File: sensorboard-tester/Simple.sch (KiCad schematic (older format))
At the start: 9 parts, among them J3 Sensor, J4 PTVoltage, J6 PTCurrent

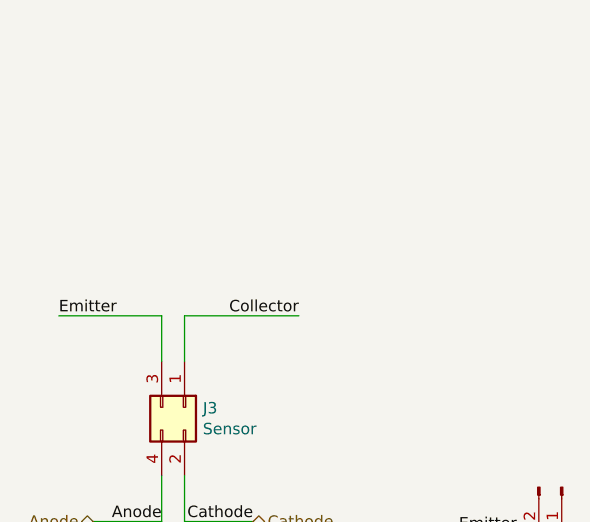
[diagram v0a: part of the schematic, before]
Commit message: Include mirrored headers for the sensorboards, in case their header has to be flipped.
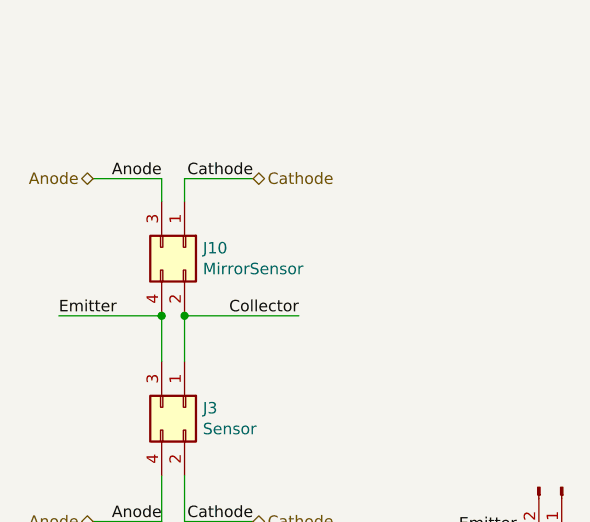
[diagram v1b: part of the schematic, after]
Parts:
- added J10: MirrorSensor, Pin_Headers:Pin_Header_Straight_2x02_Pitch2.54mm, symbol Connector_Generic:Conn_02x02_Odd_Even
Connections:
- net Anode: now also J10.3 (Pin_3)
- net Cathode: now also J10.1 (Pin_1)
- net Collector: now also J10.2 (Pin_2)
- net Emitter: now also J10.4 (Pin_4)
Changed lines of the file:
@@
 	5400 1450 5400 1250
 Connection ~ 5400 1450
+$Comp
+L Connector_Generic:Conn_02x02_Odd_Even J10
+U 1 1 5FE12BB4
+P 3600 2100
+F 0 "J10" V 3604 2180 50  0000 L CNN
+F 1 "MirrorSensor" V 3695 2180 50  0000 L CNN
+F 2 "Pin_Headers:Pin_Header_Straight_2x02_Pitch2.54mm" H 3600 2100 50  0001 C CNN
+F 3 "~" H 3600 2100 50  0001 C CNN
+	1    3600 2100
+	0    1    1    0
+$EndComp
+Connection ~ 3600 2400
+Connection ~ 3500 2400
+Wire Wire Line
+	3500 1900 3500 1800
+Wire Wire Line
+	3500 1800 3200 1800
+Wire Wire Line
+	3600 1900 3600 1800
+Wire Wire Line
+	3600 1800 3900 1800
+Text HLabel 3200 1800 0    50   BiDi ~ 0
+Anode
+Text HLabel 3900 1800 2    50   BiDi ~ 0
+Cathode
+Text Label 3900 1800 2    50   ~ 0
+Cathode
+Text Label 3500 1800 2    50   ~ 0
+Anode
 $EndSCHEMATC

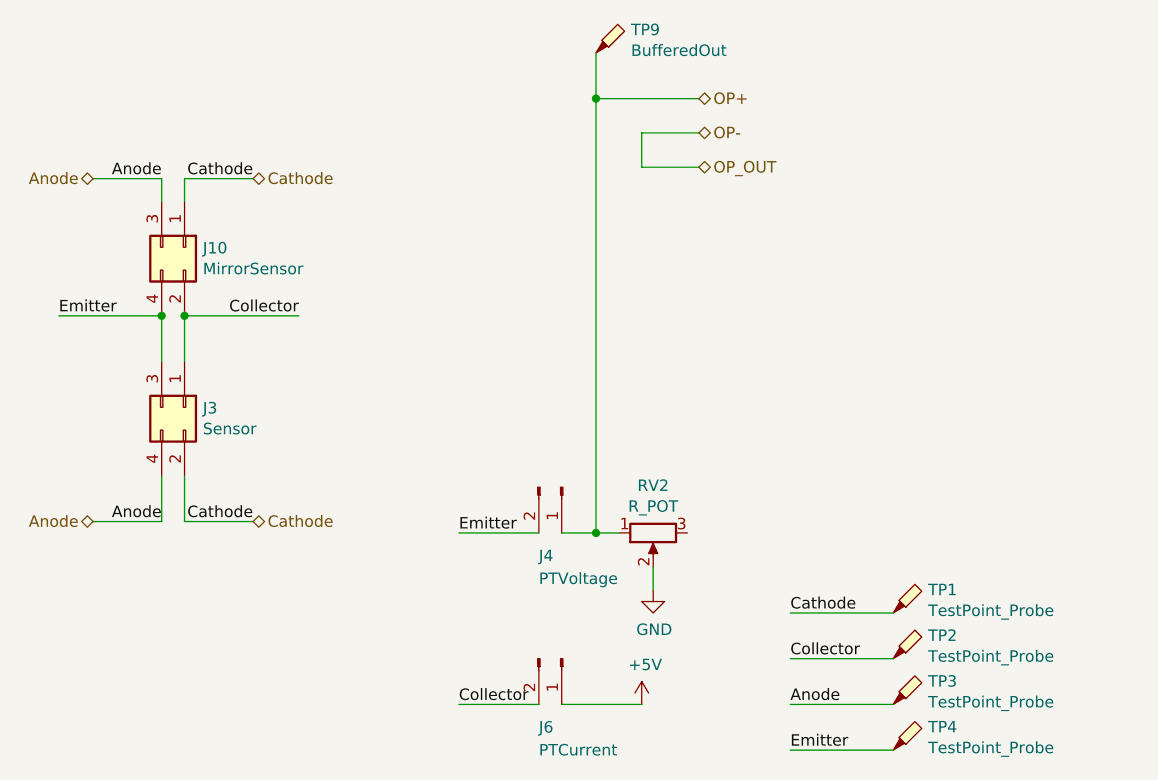
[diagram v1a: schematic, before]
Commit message: Cleanup and reconcile the headers. Switch to SOT23 regulators for both.
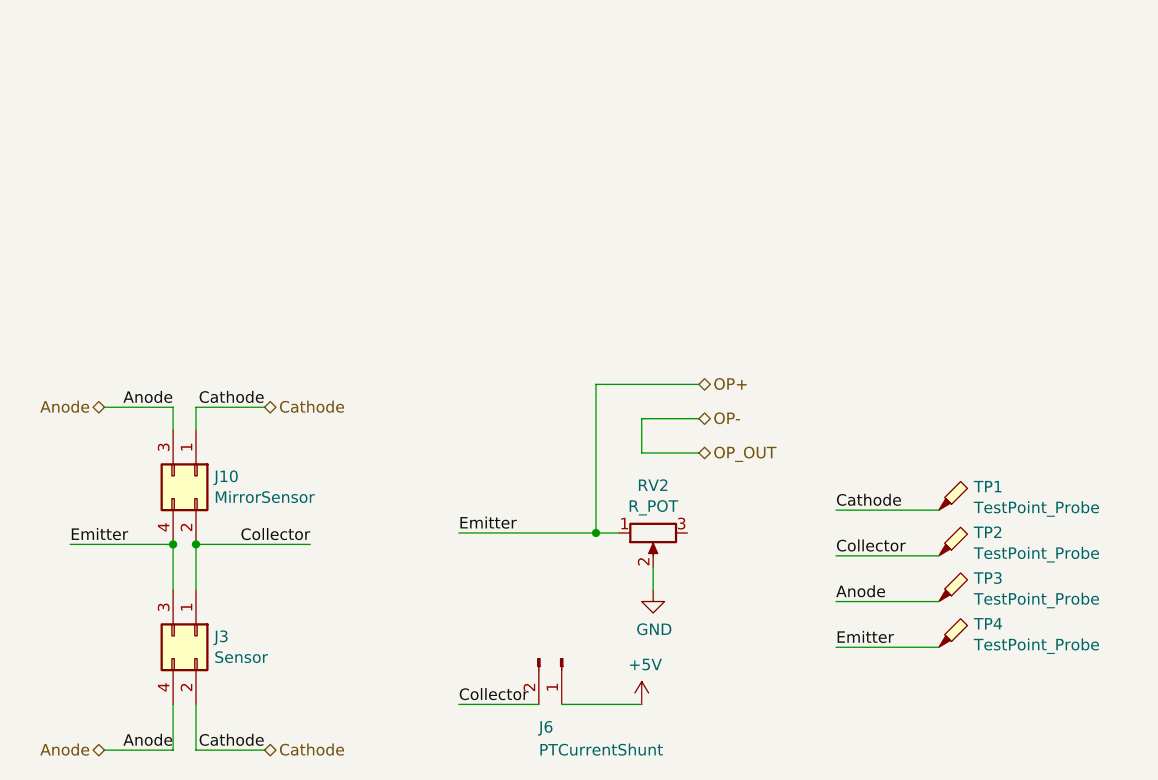
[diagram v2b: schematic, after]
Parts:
- removed J4: PTVoltage, Pin_Headers:Pin_Header_Straight_1x02_Pitch2.54mm, symbol Connector:Conn_01x02_Male
- removed TP9: BufferedOut, Pin_Headers:Pin_Header_Straight_1x01_Pitch2.54mm, symbol Connector:TestPoint_Probe
- J6: value PTCurrent -> PTCurrentShunt
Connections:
- net Emitter is gone; now on net OP+: J10.4 (Pin_4), J3.3 (Pin_3), TP4.1
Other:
- moved on the sheet: J10, J3, TP1, TP2, TP3, TP4
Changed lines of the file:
@@
 	0    -1   1    0
 $EndComp
-Wire Wire Line
-	5250 3350 5400 3350
-Wire Wire Line
-	5650 3500 5650 3600
 $Comp
 L power:GND #PWR0103
@@
 	1    0    0    -1
 $EndComp
-$Comp
-L Connector:Conn_01x02_Male J4
-U 1 1 5FC3F661
-P 5250 3150
-F 0 "J4" V 5550 3050 50  0000 L CNN
-F 1 "PTVoltage" V 5650 3050 50  0000 L CNN
-F 2 "Pin_Headers:Pin_Header_Straight_1x02_Pitch2.54mm" H 5250 3150 50  0001 C CNN
-F 3 "~" H 5250 3150 50  0001 C CNN
-	1    5250 3150
-	0    1    1    0
-$EndComp
-Wire Wire Line
-	5150 3350 4800 3350
 Text Label 4800 3350 0    50   ~ 0
 Emitter
@@
 P 5250 3900
 F 0 "J6" V 5550 3800 50  0000 L CNN
-F 1 "PTCurrent" V 5650 3800 50  0000 L CNN
+F 1 "PTCurrentShunt" V 5650 3800 50  0000 L CNN
 F 2 "Pin_Headers:Pin_Header_Straight_1x02_Pitch2.54mm" H 5250 3900 50  0001 C CNN
 F 3 "~" H 5250 3900 50  0001 C CNN
@@
 L Connector:TestPoint_Probe TP1
 U 1 1 5FC3F672
-P 6700 3700
-F 0 "TP1" H 6853 3801 50  0000 L CNN
-F 1 "TestPoint_Probe" H 6853 3710 50  0000 L CNN
-F 2 "Pin_Headers:Pin_Header_Straight_1x01_Pitch2.54mm" H 6900 3700 50  0001 C CNN
-F 3 "~" H 6900 3700 50  0001 C CNN
-	1    6700 3700
+P 6900 3250
+F 0 "TP1" H 7053 3351 50  0000 L CNN
+F 1 "TestPoint_Probe" H 7053 3260 50  0000 L CNN
+F 2 "Pin_Headers:Pin_Header_Straight_1x01_Pitch2.54mm" H 7100 3250 50  0001 C CNN
+F 3 "~" H 7100 3250 50  0001 C CNN
+	1    6900 3250
 	1    0    0    -1
 $EndComp
@@
 L Connector:TestPoint_Probe TP2
 U 1 1 5FC3F678
-P 6700 3900
-F 0 "TP2" H 6853 4001 50  0000 L CNN
-F 1 "TestPoint_Probe" H 6853 3910 50  0000 L CNN
-F 2 "Pin_Headers:Pin_Header_Straight_1x01_Pitch2.54mm" H 6900 3900 50  0001 C CNN
-F 3 "~" H 6900 3900 50  0001 C CNN
-	1    6700 3900
+P 6900 3450
+F 0 "TP2" H 7053 3551 50  0000 L CNN
+F 1 "TestPoint_Probe" H 7053 3460 50  0000 L CNN
+F 2 "Pin_Headers:Pin_Header_Straight_1x01_Pitch2.54mm" H 7100 3450 50  0001 C CNN
+F 3 "~" H 7100 3450 50  0001 C CNN
+	1    6900 3450
 	1    0    0    -1
 $EndComp
@@
 L Connector:TestPoint_Probe TP3
 U 1 1 5FC3F67E
-P 6700 4100
-F 0 "TP3" H 6853 4201 50  0000 L CNN
-F 1 "TestPoint_Probe" H 6853 4110 50  0000 L CNN
-F 2 "Pin_Headers:Pin_Header_Straight_1x01_Pitch2.54mm" H 6900 4100 50  0001 C CNN
-F 3 "~" H 6900 4100 50  0001 C CNN
-	1    6700 4100
+P 6900 3650
+F 0 "TP3" H 7053 3751 50  0000 L CNN
+F 1 "TestPoint_Probe" H 7053 3660 50  0000 L CNN
+F 2 "Pin_Headers:Pin_Header_Straight_1x01_Pitch2.54mm" H 7100 3650 50  0001 C CNN
+F 3 "~" H 7100 3650 50  0001 C CNN
+	1    6900 3650
 	1    0    0    -1
 $EndComp
@@
 L Connector:TestPoint_Probe TP4
 U 1 1 5FC3F684
-P 6700 4300
-F 0 "TP4" H 6853 4401 50  0000 L CNN
-F 1 "TestPoint_Probe" H 6853 4310 50  0000 L CNN
-F 2 "Pin_Headers:Pin_Header_Straight_1x01_Pitch2.54mm" H 6900 4300 50  0001 C CNN
-F 3 "~" H 6900 4300 50  0001 C CNN
-	1    6700 4300
+P 6900 3850
+F 0 "TP4" H 7053 3951 50  0000 L CNN
+F 1 "TestPoint_Probe" H 7053 3860 50  0000 L CNN
+F 2 "Pin_Headers:Pin_Header_Straight_1x01_Pitch2.54mm" H 7100 3850 50  0001 C CNN
+F 3 "~" H 7100 3850 50  0001 C CNN
+	1    6900 3850
 	1    0    0    -1
 $EndComp
 Wire Wire Line
-	6700 3700 6250 3700
+	6900 3250 6450 3250
 Wire Wire Line
-	6700 3900 6250 3900
+	6900 3450 6450 3450
 Wire Wire Line
-	6700 4100 6250 4100
+	6900 3650 6450 3650
 Wire Wire Line
-	6700 4300 6250 4300
-Text Label 6250 3700 0    50   ~ 0
+	6900 3850 6450 3850
+Text Label 6450 3250 0    50   ~ 0
 Cathode
-Text Label 6250 3900 0    50   ~ 0
+Text Label 6450 3450 0    50   ~ 0
 Collector
-Text Label 6250 4100 0    50   ~ 0
+Text Label 6450 3650 0    50   ~ 0
 Anode
-Text Label 6250 4300 0    50   ~ 0
+Text Label 6450 3850 0    50   ~ 0
 Emitter
 $Comp
 L Connector_Generic:Conn_02x02_Odd_Even J3
 U 1 1 5FC3F692
-P 3600 2800
-F 0 "J3" V 3604 2880 50  0000 L CNN
-F 1 "Sensor" V 3695 2880 50  0000 L CNN
-F 2 "Pin_Headers:Pin_Header_Straight_2x02_Pitch2.54mm" H 3600 2800 50  0001 C CNN
-F 3 "~" H 3600 2800 50  0001 C CNN
-	1    3600 2800
+P 3650 3800
+F 0 "J3" V 3654 3880 50  0000 L CNN
+F 1 "Sensor" V 3745 3880 50  0000 L CNN
+F 2 "Pin_Headers:Pin_Header_Straight_2x02_Pitch2.54mm" H 3650 3800 50  0001 C CNN
+F 3 "~" H 3650 3800 50  0001 C CNN
+	1    3650 3800
 	0    1    1    0
 $EndComp
 Wire Wire Line
-	3600 2600 3600 2400
+	3650 3600 3650 3400
 Wire Wire Line
-	3600 2400 4100 2400
+	3650 3400 4150 3400
 Wire Wire Line
-	3500 2600 3500 2400
+	3550 3600 3550 3400
 Wire Wire Line
-	3500 2400 3050 2400
+	3550 3400 3100 3400
 Wire Wire Line
-	3500 3100 3500 3300
+	3550 4100 3550 4300
 Wire Wire Line
-	3500 3300 3200 3300
+	3550 4300 3250 4300
 Wire Wire Line
-	3600 3100 3600 3300
+	3650 4100 3650 4300
 Wire Wire Line
-	3600 3300 3900 3300
-Text Label 3050 2400 0    50   ~ 0
+	3650 4300 3950 4300
+Text Label 3100 3400 0    50   ~ 0
 Emitter
-Text Label 4100 2400 2    50   ~ 0
+Text Label 4150 3400 2    50   ~ 0
 Collector
 $Comp
@@
 	1    0    0    -1
 $EndComp
-Text HLabel 5850 1450 2    50   BiDi ~ 0
+Text HLabel 5850 2700 2    50   BiDi ~ 0
 OP+
-Text HLabel 5850 1600 2    50   BiDi ~ 0
+Text HLabel 5850 2850 2    50   BiDi ~ 0
 OP-
-Text HLabel 5850 1750 2    50   BiDi ~ 0
+Text HLabel 5850 3000 2    50   BiDi ~ 0
 OP_OUT
-Text HLabel 3200 3300 0    50   BiDi ~ 0
+Text HLabel 3250 4300 0    50   BiDi ~ 0
 Anode
-Text HLabel 3900 3300 2    50   BiDi ~ 0
+Text HLabel 3950 4300 2    50   BiDi ~ 0
 Cathode
-Text Label 3900 3300 2    50   ~ 0
+Text Label 3950 4300 2    50   ~ 0
 Cathode
-Text Label 3500 3300 2    50   ~ 0
+Text Label 3550 4300 2    50   ~ 0
 Anode
 Wire Wire Line
-	5850 1600 5600 1600
+	5850 2850 5600 2850
 Wire Wire Line
-	5600 1600 5600 1750
+	5600 2850 5600 3000
 Wire Wire Line
-	5600 1750 5850 1750
+	5600 3000 5850 3000
 Wire Wire Line
-	5400 3350 5400 1450
+	5400 3350 5400 2700
 Wire Wire Line
-	5400 1450 5850 1450
+	5400 2700 5850 2700
 Connection ~ 5400 3350
 Wire Wire Line
 	5400 3350 5500 3350
 $Comp
-L Connector:TestPoint_Probe TP9
-U 1 1 5FC933E2
-P 5400 1250
-F 0 "TP9" H 5553 1351 50  0000 L CNN
-F 1 "BufferedOut" H 5553 1260 50  0000 L CNN
-F 2 "Pin_Headers:Pin_Header_Straight_1x01_Pitch2.54mm" H 5600 1250 50  0001 C CNN
-F 3 "~" H 5600 1250 50  0001 C CNN
-	1    5400 1250
-	1    0    0    -1
-$EndComp
-Wire Wire Line
-	5400 1450 5400 1250
-Connection ~ 5400 1450
-$Comp
 L Connector_Generic:Conn_02x02_Odd_Even J10
 U 1 1 5FE12BB4
-P 3600 2100
-F 0 "J10" V 3604 2180 50  0000 L CNN
-F 1 "MirrorSensor" V 3695 2180 50  0000 L CNN
-F 2 "Pin_Headers:Pin_Header_Straight_2x02_Pitch2.54mm" H 3600 2100 50  0001 C CNN
-F 3 "~" H 3600 2100 50  0001 C CNN
-	1    3600 2100
+P 3650 3100
+F 0 "J10" V 3654 3180 50  0000 L CNN
+F 1 "MirrorSensor" V 3745 3180 50  0000 L CNN
+F 2 "Pin_Headers:Pin_Header_Straight_2x02_Pitch2.54mm" H 3650 3100 50  0001 C CNN
+F 3 "~" H 3650 3100 50  0001 C CNN
+	1    3650 3100
 	0    1    1    0
 $EndComp
-Connection ~ 3600 2400
-Connection ~ 3500 2400
+Connection ~ 3650 3400
+Connection ~ 3550 3400
 Wire Wire Line
-	3500 1900 3500 1800
+	3550 2900 3550 2800
 Wire Wire Line
-	3500 1800 3200 1800
+	3550 2800 3250 2800
 Wire Wire Line
-	3600 1900 3600 1800
+	3650 2900 3650 2800
 Wire Wire Line
-	3600 1800 3900 1800
-Text HLabel 3200 1800 0    50   BiDi ~ 0
+	3650 2800 3950 2800
+Text HLabel 3250 2800 0    50   BiDi ~ 0
 Anode
-Text HLabel 3900 1800 2    50   BiDi ~ 0
+Text HLabel 3950 2800 2    50   BiDi ~ 0
 Cathode
-Text Label 3900 1800 2    50   ~ 0
+Text Label 3950 2800 2    50   ~ 0
 Cathode
-Text Label 3500 1800 2    50   ~ 0
+Text Label 3550 2800 2    50   ~ 0
 Anode
+Wire Wire Line
+	4800 3350 5400 3350
+Wire Wire Line
+	5650 3500 5650 3600
 $EndSCHEMATC
